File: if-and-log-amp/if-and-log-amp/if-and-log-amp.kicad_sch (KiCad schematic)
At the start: 59 parts

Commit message: if and log amp routing and 3d model
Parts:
- added H301, H302, H303, H304: MountingHole, MountingHole:MountingHole_3.2mm_M3, symbol Mechanical:MountingHole
- added J302, J303, J304, J305, J306: Conn_01x01_Male, Connector_Wire:SolderWire-0.15sqmm_1x01_D0.5mm_OD1.5mm, symbol Connector:Conn_01x01_Male
- C315: value (none) -> 50p; footprint (none) -> if-log-amp:GKG60015
- C316: footprint (none) -> Capacitor_THT:C_Radial_D4.0mm_H5.0mm_P1.50mm
- D301: value (none) -> 1N4152; footprint (none) -> Diode_THT:D_DO-35_SOD27_P7.62mm_Horizontal
- J301: value (none) -> Conn_Coaxial; footprint (none) -> if-log-amp:TE_5-1634503-1
- L301: footprint (none) -> Inductor_THT:L_Toroid_Horizontal_D12.7mm_P20.00mm_Diameter14-5mm_Amidon-T50
- RV301: value (none) -> 10k
- RV303: renamed from R322; value (none) -> 10k
- U301: value (none) -> AD603AQ; footprint (none) -> if-log-amp:AD603AQ
- U302: value (none) -> L78L05_TO92; footprint (none) -> Package_TO_SOT_THT:TO-92_Inline
- U303: value (none) -> LM317L_TO92; footprint (none) -> Package_TO_SOT_THT:TO-92_Inline
- U304: value (none) -> AD8307AN; footprint (none) -> if-log-amp:AD8307AN
- U305: value (none) -> CA3140; footprint CA3140EZ:CA3140EZ -> if-log-amp:CA3140EZ
- V301: value (none) -> +15
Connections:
- net GND: now also U301.6 (VNEG); no longer U301.50 (VNEG)
- net at C302.3, R308.2: now also J303.1 (Pin_1)
- net at C301.3, R304.2, R305.1: now also J302.1 (Pin_1)
- net at C303.3, R305.2, R306.1: now also J304.1 (Pin_1)
- net at C307.1, R308.1: now also U301.1 (GPOS); no longer U301.40 (GPOS)
- net at C312.2, R312.2: now also U301.8 (VPOS); no longer U301.99 (VPOS)
- net at C323.1, R321.2: now also J306.1 (Pin_1)
- net at C324.1, R319.2: now also J305.1 (Pin_1)
- net at C306.1, R307.2: now also U301.4 (COMM); no longer U301.2 (COMM)
- net at C308.1, R309.1: now also U301.2 (GNEG); no longer U301.41 (GNEG)
- net at C311.1: now also U301.5 (FDBK); no longer U301.49 (FDBK)
- net at R313.1: now also U301.7 (VOUT); no longer U301.48 (VOUT)
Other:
- moved on the sheet: R321

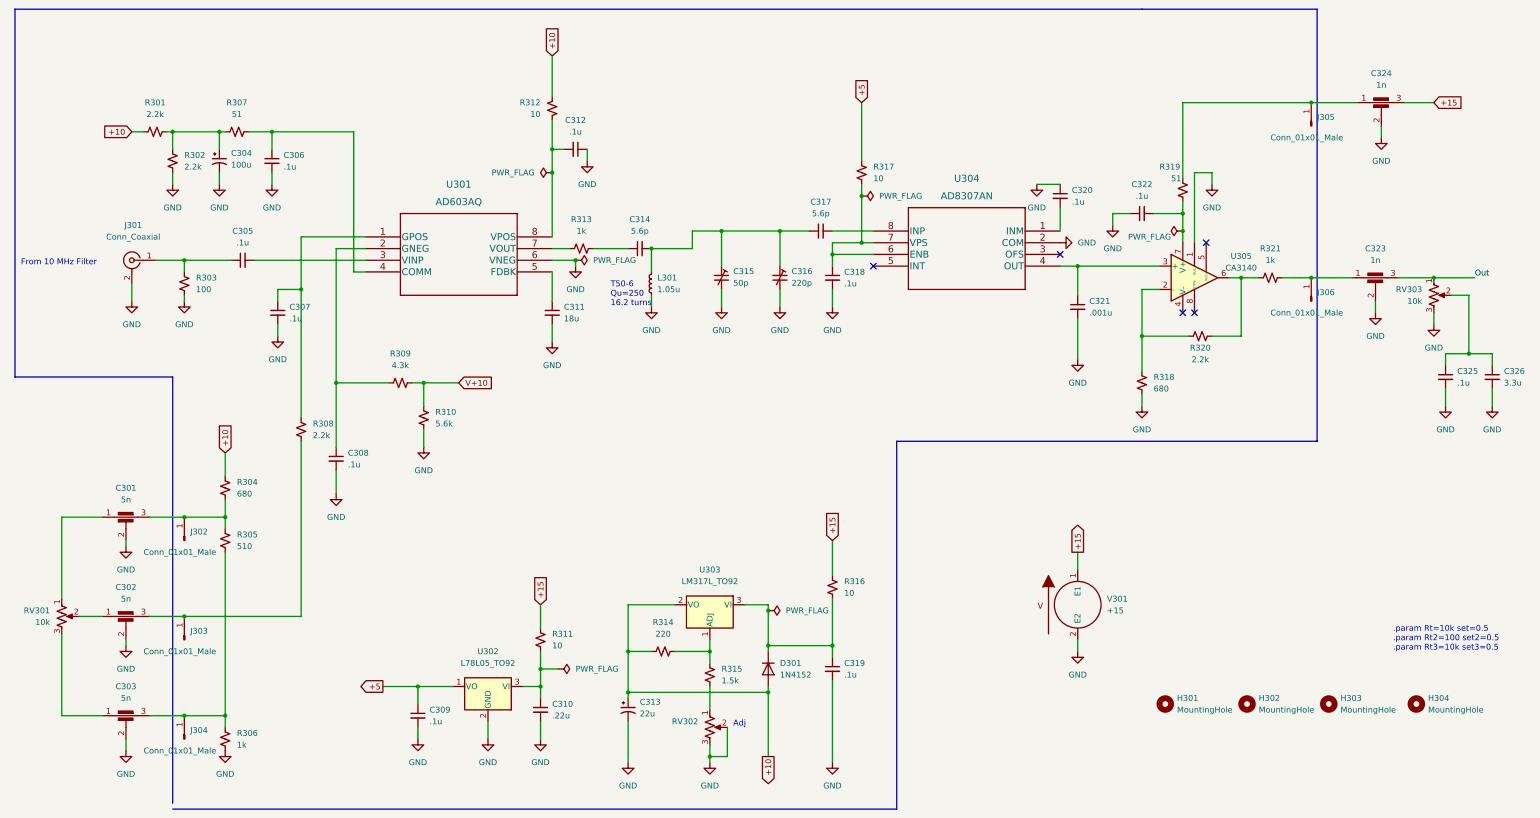
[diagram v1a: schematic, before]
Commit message: Improvements to if and log amp
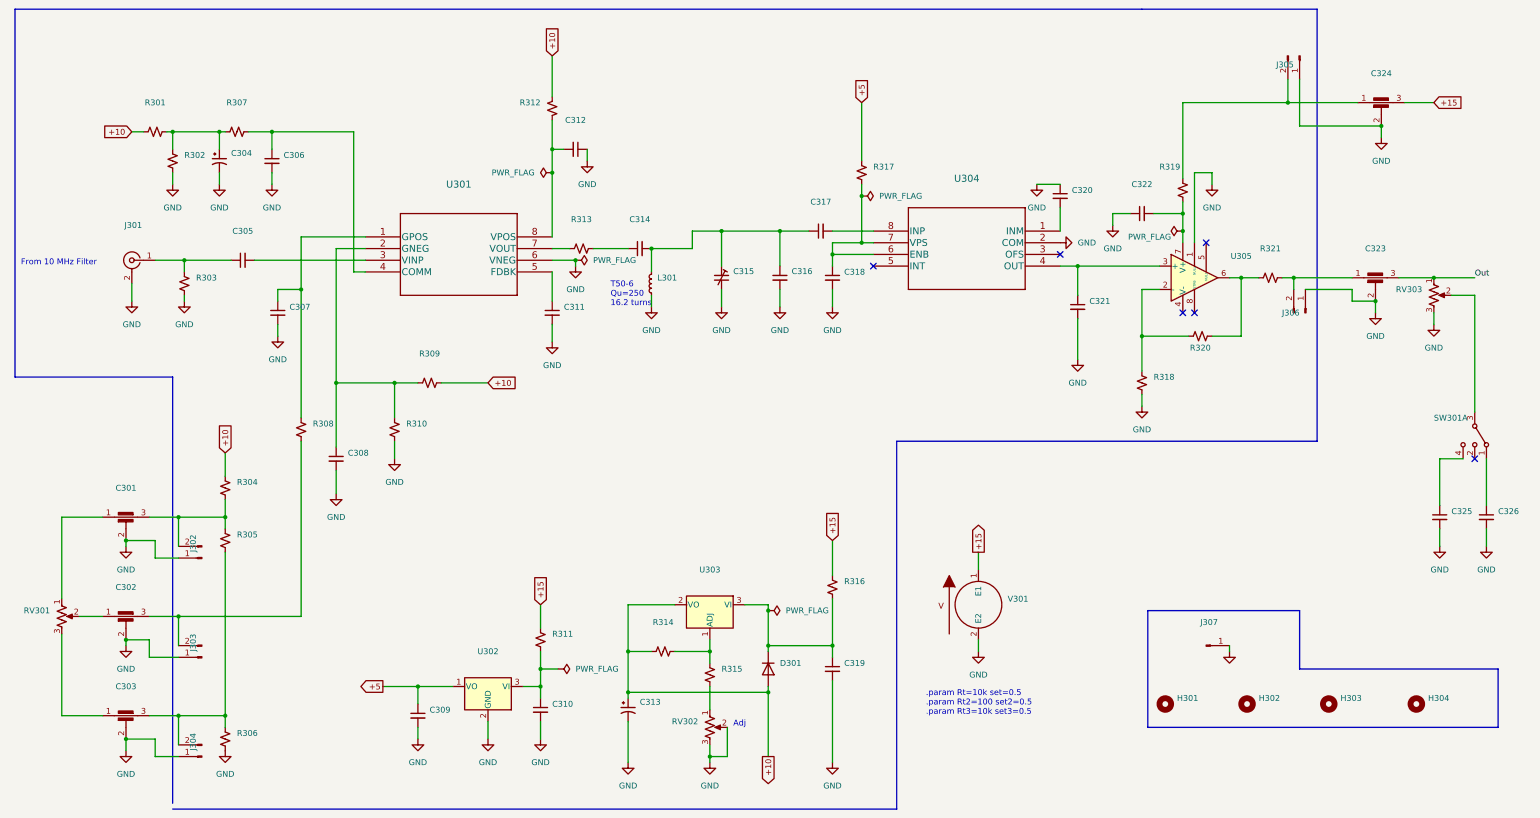
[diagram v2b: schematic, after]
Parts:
- added J307: (no value), symbol Connector:Conn_01x01_Male
- added SW301: (no value), symbol Switch:SW_DP3T
- C301, C302, C303: value 5n -> (none)
- C304: value 100u -> (none); footprint Capacitor_THT:CP_Axial_L11.0mm_D6.0mm_P18.00mm_Horizontal -> (none)
- C305, C306, C307, C308, C309, C312, C318, C319, C320, C322: value .1u -> (none); footprint Capacitor_THT:C_Radial_D4.0mm_H5.0mm_P1.50mm -> (none)
- C310: value .22u -> (none); footprint Capacitor_THT:C_Radial_D4.0mm_H5.0mm_P1.50mm -> (none)
- C311: value 18u -> (none); footprint Capacitor_THT:C_Radial_D4.0mm_H5.0mm_P1.50mm -> (none)
- C313: value 22u -> (none); footprint Capacitor_THT:CP_Axial_L11.0mm_D6.0mm_P18.00mm_Horizontal -> (none)
- C314, C317: value 5.6p -> (none); footprint Capacitor_THT:C_Radial_D4.0mm_H5.0mm_P1.50mm -> (none)
- C315: value 50p -> (none); footprint if-log-amp:GKG60015 -> (none)
- C316: value 220p -> (none); footprint Capacitor_THT:C_Radial_D4.0mm_H5.0mm_P1.50mm -> (none); symbol Device:C_Trim_Small -> Device:C_Small
- C321: value .001u -> (none); footprint Capacitor_THT:C_Radial_D4.0mm_H5.0mm_P1.50mm -> (none)
- C323, C324: value 1n -> (none)
- C325: value .1u -> (none)
- C326: value 3.3u -> (none)
- D301: value 1N4152 -> (none); footprint Diode_THT:D_DO-35_SOD27_P7.62mm_Horizontal -> (none)
- H301, H302, H303, H304: value MountingHole -> (none); footprint MountingHole:MountingHole_3.2mm_M3 -> (none)
- J301: value Conn_Coaxial -> (none); footprint if-log-amp:TE_5-1634503-1 -> (none)
- J302, J303, J304, J305, J306: value Conn_01x01_Male -> (none); footprint Connector_Wire:SolderWire-0.15sqmm_1x01_D0.5mm_OD1.5mm -> (none); symbol Connector:Conn_01x01_Male -> Connector:Conn_01x02_Male
- L301: value 1.05u -> (none); footprint Inductor_THT:L_Toroid_Horizontal_D12.7mm_P20.00mm_Diameter14-5mm_Amidon-T50 -> (none)
- R301, R302, R308, R320: value 2.2k -> (none); footprint Resistor_THT:R_Axial_DIN0207_L6.3mm_D2.5mm_P7.62mm_Horizontal -> (none)
- R303: value 100 -> (none); footprint Resistor_THT:R_Axial_DIN0207_L6.3mm_D2.5mm_P7.62mm_Horizontal -> (none)
- R304, R318: value 680 -> (none); footprint Resistor_THT:R_Axial_DIN0207_L6.3mm_D2.5mm_P7.62mm_Horizontal -> (none)
- R305: value 510 -> (none); footprint Resistor_THT:R_Axial_DIN0207_L6.3mm_D2.5mm_P7.62mm_Horizontal -> (none)
- R306, R313, R321: value 1k -> (none); footprint Resistor_THT:R_Axial_DIN0207_L6.3mm_D2.5mm_P7.62mm_Horizontal -> (none)
- R307, R319: value 51 -> (none); footprint Resistor_THT:R_Axial_DIN0207_L6.3mm_D2.5mm_P7.62mm_Horizontal -> (none)
- R309: value 4.3k -> (none); footprint Resistor_THT:R_Axial_DIN0207_L6.3mm_D2.5mm_P7.62mm_Horizontal -> (none)
- R310: value 5.6k -> (none); footprint Resistor_THT:R_Axial_DIN0207_L6.3mm_D2.5mm_P7.62mm_Horizontal -> (none)
- R311, R312, R316, R317: value 10 -> (none); footprint Resistor_THT:R_Axial_DIN0207_L6.3mm_D2.5mm_P7.62mm_Horizontal -> (none)
- R314: value 220 -> (none); footprint Resistor_THT:R_Axial_DIN0207_L6.3mm_D2.5mm_P7.62mm_Horizontal -> (none)
- R315: value 1.5k -> (none); footprint Resistor_THT:R_Axial_DIN0207_L6.3mm_D2.5mm_P7.62mm_Horizontal -> (none)
- RV301, RV303: value 10k -> (none)
- U301: value AD603AQ -> (none); footprint if-log-amp:AD603AQ -> (none)
- U302: value L78L05_TO92 -> (none); footprint Package_TO_SOT_THT:TO-92_Inline -> (none)
- U303: value LM317L_TO92 -> (none); footprint Package_TO_SOT_THT:TO-92_Inline -> (none)
- U304: value AD8307AN -> (none); footprint if-log-amp:AD8307AN -> (none)
- U305: value CA3140 -> (none); footprint if-log-amp:CA3140EZ -> (none)
- V301: value +15 -> (none)
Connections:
- net +10: now also R309.2
- net GND: now also J302.1 (Pin_1), J303.1 (Pin_1), J304.1 (Pin_1), J305.1 (Pin_1), J306.1 (Pin_1), J307.1 (Pin_1)
- net at C323.1, R321.2: now also J306.2 (Pin_2); no longer J306.1 (Pin_1)
- net at C303.3, R305.2, R306.1: now also J304.2 (Pin_2); no longer J304.1 (Pin_1)
- net at C302.3, R308.2: now also J303.2 (Pin_2); no longer J303.1 (Pin_1)
- net at C301.3, R304.2, R305.1: now also J302.2 (Pin_2); no longer J302.1 (Pin_1)
- net at C324.1, R319.2: now also J305.2 (Pin_2); no longer J305.1 (Pin_1)
- net at C308.1, R309.1, U301.2 (GNEG): now also R310.1
- removed net V+10: R309.2, R310.1
- new net: C326.1, SW301.1
- new net: RV303.2, SW301.3
- new net: C325.1, SW301.4
- no-connect marks 5 -> 6
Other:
- moved on the sheet: C325, C326, R309, R310, V301

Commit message: changed 220p cap back to variable
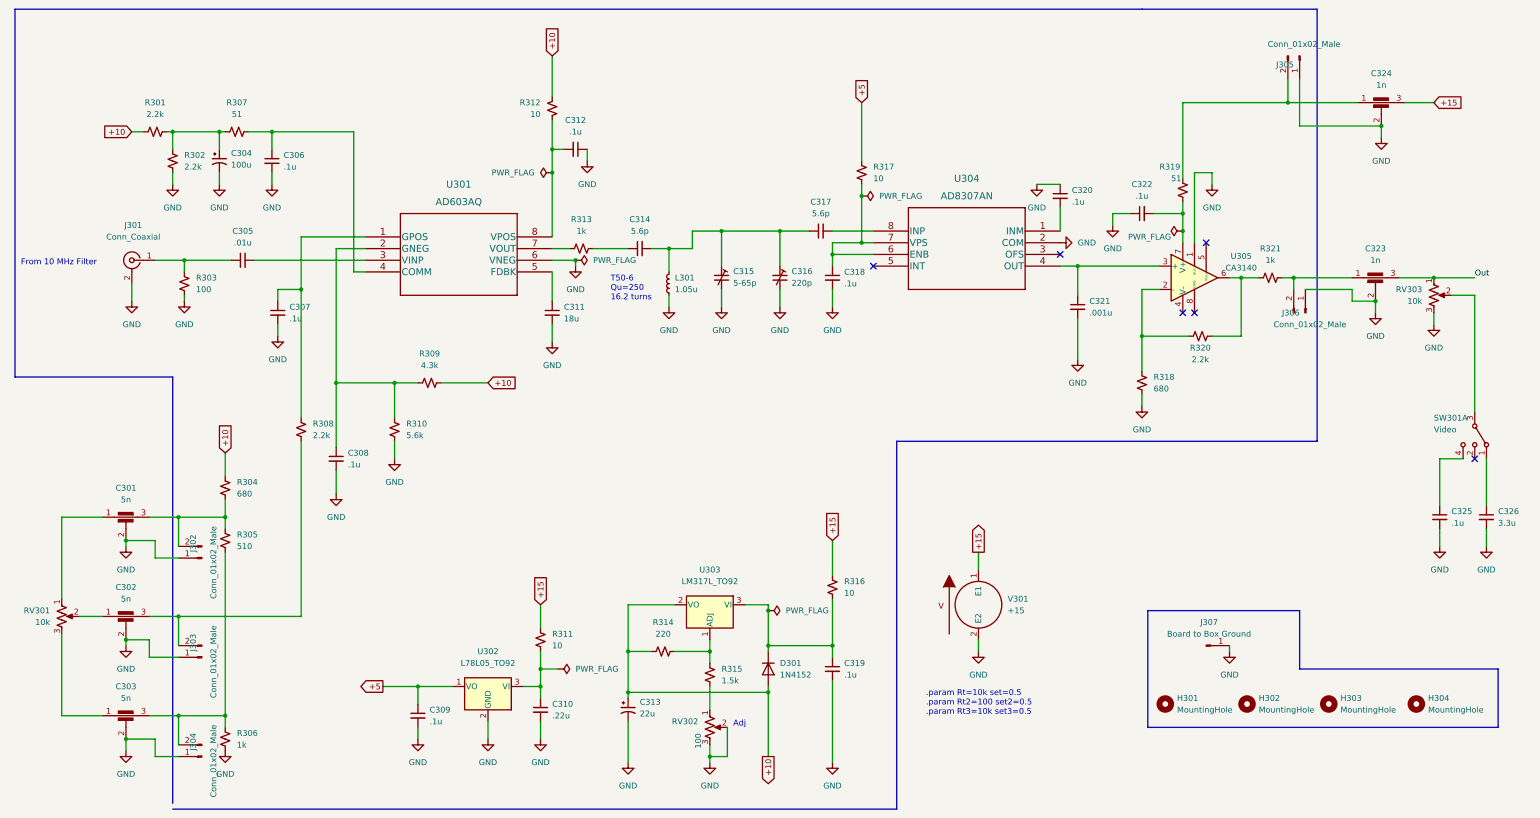
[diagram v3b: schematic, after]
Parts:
- C301, C302, C303: value (none) -> 5n
- C304: value (none) -> 100u; footprint (none) -> Capacitor_THT:CP_Radial_D5.0mm_P2.50mm
- C305: value (none) -> .01u; footprint (none) -> Capacitor_THT:C_Radial_D4.0mm_H5.0mm_P1.50mm
- C306, C307, C308, C309, C312, C318, C319, C320, C322: value (none) -> .1u; footprint (none) -> Capacitor_THT:C_Radial_D4.0mm_H5.0mm_P1.50mm
- C310: value (none) -> .22u; footprint (none) -> Capacitor_THT:C_Radial_D4.0mm_H5.0mm_P1.50mm
- C311: value (none) -> 18u; footprint (none) -> Capacitor_THT:C_Radial_D4.0mm_H5.0mm_P1.50mm
- C313: value (none) -> 22u; footprint (none) -> Capacitor_THT:CP_Radial_D5.0mm_P2.50mm
- C314, C317: value (none) -> 5.6p; footprint (none) -> Capacitor_THT:C_Radial_D4.0mm_H5.0mm_P1.50mm
- C315: value (none) -> 5-65p; footprint (none) -> if-log-amp:GKG60015
- C316: value (none) -> 220p; footprint (none) -> Capacitor_THT:C_Radial_D4.0mm_H5.0mm_P1.50mm; symbol Device:C_Small -> Device:C_Trim_Small
- C321: value (none) -> .001u; footprint (none) -> Capacitor_THT:C_Radial_D4.0mm_H5.0mm_P1.50mm
- C323, C324: value (none) -> 1n
- C325: value (none) -> .1u
- C326: value (none) -> 3.3u
- D301: value (none) -> 1N4152; footprint (none) -> Diode_THT:D_DO-35_SOD27_P7.62mm_Horizontal
- H301, H302, H303, H304: value (none) -> MountingHole; footprint (none) -> MountingHole:MountingHole_3.2mm_M3
- J301: value (none) -> Conn_Coaxial; footprint (none) -> Connector_Wire:SolderWire-0.15sqmm_1x02_P4mm_D0.5mm_OD1.5mm
- J302, J303, J304, J305, J306: value (none) -> Conn_01x02_Male; footprint (none) -> Connector_Wire:SolderWire-0.15sqmm_1x02_P4mm_D0.5mm_OD1.5mm
- J307: value (none) -> Board to Box Ground; footprint (none) -> Connector_Wire:SolderWire-0.15sqmm_1x01_D0.5mm_OD1.5mm
- L301: value (none) -> 1.05u; footprint (none) -> Inductor_THT:L_Toroid_Vertical_L13.0mm_W6.5mm_P5.60mm
- R301, R302, R308, R320: value (none) -> 2.2k; footprint (none) -> Resistor_THT:R_Axial_DIN0207_L6.3mm_D2.5mm_P7.62mm_Horizontal
- R303: value (none) -> 100; footprint (none) -> Resistor_THT:R_Axial_DIN0207_L6.3mm_D2.5mm_P7.62mm_Horizontal
- R304, R318: value (none) -> 680; footprint (none) -> Resistor_THT:R_Axial_DIN0207_L6.3mm_D2.5mm_P7.62mm_Horizontal
- R305: value (none) -> 510; footprint (none) -> Resistor_THT:R_Axial_DIN0207_L6.3mm_D2.5mm_P7.62mm_Horizontal
- R306, R313, R321: value (none) -> 1k; footprint (none) -> Resistor_THT:R_Axial_DIN0207_L6.3mm_D2.5mm_P7.62mm_Horizontal
- R307, R319: value (none) -> 51; footprint (none) -> Resistor_THT:R_Axial_DIN0207_L6.3mm_D2.5mm_P7.62mm_Horizontal
- R309: value (none) -> 4.3k; footprint (none) -> Resistor_THT:R_Axial_DIN0207_L6.3mm_D2.5mm_P7.62mm_Horizontal
- R310: value (none) -> 5.6k; footprint (none) -> Resistor_THT:R_Axial_DIN0207_L6.3mm_D2.5mm_P7.62mm_Horizontal
- R311, R312, R316, R317: value (none) -> 10; footprint (none) -> Resistor_THT:R_Axial_DIN0207_L6.3mm_D2.5mm_P7.62mm_Horizontal
- R314: value (none) -> 220; footprint (none) -> Resistor_THT:R_Axial_DIN0207_L6.3mm_D2.5mm_P7.62mm_Horizontal
- R315: value (none) -> 1.5k; footprint (none) -> Resistor_THT:R_Axial_DIN0207_L6.3mm_D2.5mm_P7.62mm_Horizontal
- RV301, RV303: value (none) -> 10k
- RV302: value (none) -> 100; footprint (none) -> if-log-amp:Potentiometer_Bourns_3386G_Vertical
- SW301: value (none) -> Video
- U301: value (none) -> AD603AQ; footprint (none) -> if-log-amp:AD603AQ
- U302: value (none) -> L78L05_TO92; footprint (none) -> Package_TO_SOT_THT:TO-92_Inline
- U303: value (none) -> LM317L_TO92; footprint (none) -> Package_TO_SOT_THT:TO-92_Inline
- U304: value (none) -> AD8307AN; footprint (none) -> if-log-amp:AD8307AN
- U305: value (none) -> CA3140; footprint (none) -> if-log-amp:CA3140EZ
- V301: value (none) -> +15
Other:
- moved on the sheet: L301
